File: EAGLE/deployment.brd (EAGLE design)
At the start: 160 x 100 mm, 7 parts, among them Q1 100V 14A

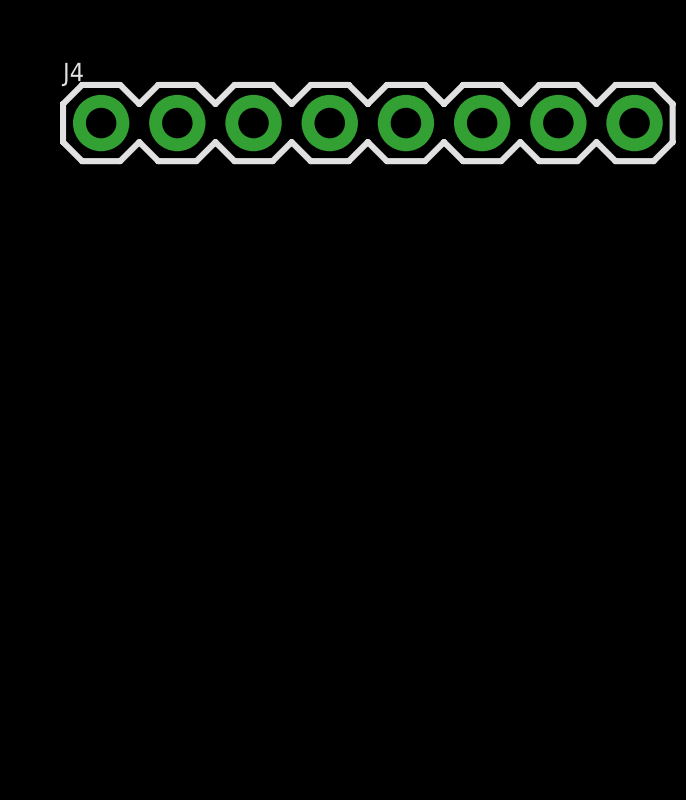
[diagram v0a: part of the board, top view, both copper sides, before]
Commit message: Added nichrome wire circuit to deployment schematic
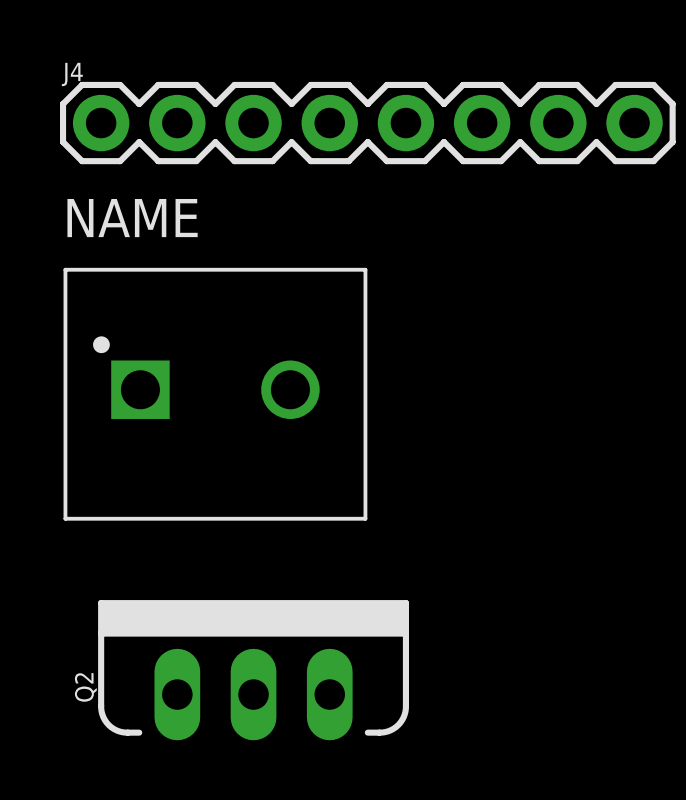
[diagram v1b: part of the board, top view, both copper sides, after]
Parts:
- added J5: (no value), 1935161:PHOENIX_1935161
- added Q2: 100V 14A, SparkFun-DiscreteSemi:TO220V
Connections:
- new net N$2: J5.1, Q2.3
- net 2: now also Q2.1
- net 9V: now also J5.2
- net GND: now also Q2.2
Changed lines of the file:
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@@
 <attribute name="VALUE" x="-53.34" y="-52.832" size="0.6096" layer="27" font="vector" ratio="20"/>
+</element>
+<element name="Q2" library="SparkFun-DiscreteSemi" library_urn="urn:adsk.eagle:library:514" package="TO220V" package3d_urn="urn:adsk.eagle:package:38447/1" value="100V 14A" x="-46.99" y="-69.85" smashed="yes">
+<attribute name="NAME" x="-52.324" y="-69.596" size="0.6096" layer="25" font="vector" ratio="20" rot="R90" align="bottom-center"/>
+<attribute name="PROD_ID" value="TRANS-10060" x="-46.99" y="-55.88" size="1.778" layer="27" display="off"/>
+<attribute name="VALUE" x="-41.656" y="-69.596" size="0.6096" layer="27" font="vector" ratio="20" rot="R90" align="top-center"/>
+</element>
+<element name="J5" library="1935161" package="PHOENIX_1935161" value="" x="-48.26" y="-59.69" smashed="yes">
+<attribute name="DESCRIPTION" value=" Conn Terminal Blocks 2 POS 5mm Solder ST Thru-Hole 16A " x="-59.69" y="-50.8" size="1.778" layer="27" display="off"/>
+<attribute name="DIGI-KEY_PART_NUMBER" value="277-1667-ND" x="-59.69" y="-50.8" size="1.778" layer="27" display="off"/>
+<attribute name="DIGI-KEY_PURCHASE_URL" value="https://www.digikey.com/product-detail/en/phoenix-contact/1935161/277-1667-ND/568614?utm_source=snapeda&amp;utm_medium=aggregator&amp;utm_campaign=symbol" x="-59.69" y="-50.8" size="1.778" layer="27" display="off"/>
+<attribute name="MF" value="Phoenix Contact" x="-59.69" y="-50.8" size="1.778" layer="27" display="off"/>
+<attribute name="MP" value="1935161" x="-59.69" y="-50.8" size="1.778" layer="27" display="off"/>
+<attribute name="PACKAGE" value="None" x="-59.69" y="-50.8" size="1.778" layer="27" display="off"/>
 </element>
 </elements>
@@
 <contactref element="Q1" pad="2"/>
 <contactref element="J4" pad="6"/>
+<contactref element="Q2" pad="2"/>
+<wire x1="-39.37" y1="-50.8" x2="-46.99" y2="-69.85" width="0" layer="19" extent="1-1"/>
 <wire x1="-45.76" y1="-40.64" x2="-39.37" y2="-50.8" width="0" layer="19" extent="1-1"/>
 <wire x1="-46.99" y1="-3.81" x2="-45.76" y2="-40.64" width="0" layer="19" extent="1-1"/>
@@
 <contactref element="JP3" pad="12"/>
 <contactref element="Q1" pad="1"/>
+<contactref element="Q2" pad="1"/>
+<wire x1="-49.53" y1="-3.81" x2="-49.53" y2="-69.85" width="0" layer="19" extent="1-1"/>
 <wire x1="-13.97" y1="6.35" x2="-49.53" y2="-3.81" width="0" layer="19" extent="1-1"/>
 </signal>
@@
 <contactref element="J1" pad="2"/>
 <contactref element="J2" pad="1"/>
+<contactref element="J5" pad="2"/>
+<wire x1="-50.76" y1="-26.67" x2="-45.76" y2="-59.69" width="0" layer="19" extent="1-1"/>
 <wire x1="-45.76" y1="-12.7" x2="-50.76" y2="-26.67" width="0" layer="19" extent="1-1"/>
 </signal>
@@
 <contactref element="J4" pad="8"/>
 </signal>
+<signal name="N$2">
+<contactref element="J5" pad="1"/>
+<contactref element="Q2" pad="3"/>
+<wire x1="-50.76" y1="-59.69" x2="-44.45" y2="-69.85" width="0" layer="19" extent="1-1"/>
+</signal>
 </signals>
